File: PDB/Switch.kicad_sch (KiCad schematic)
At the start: 27 parts, among them U1 BTH50030-1LUA, U10 BTH50030-1LUA, U11 74LVC1G175, U12 74LVC1G175, U13 TLV809EA29DBZR, U14 LM4040CELT-3.0, U15 LM4040CELT-3.0

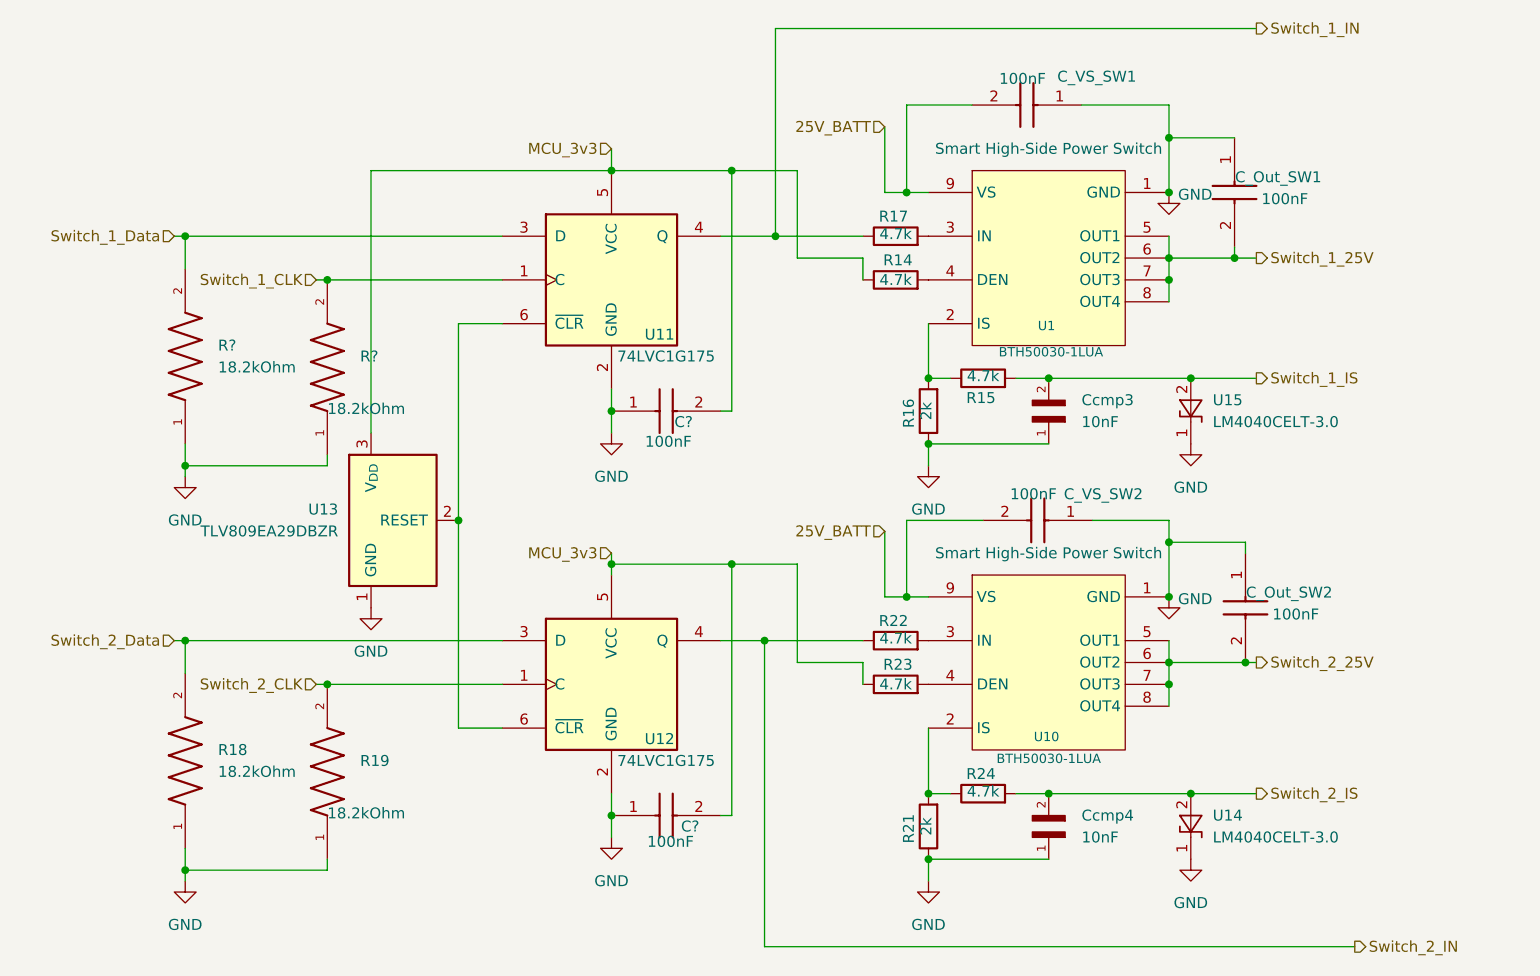
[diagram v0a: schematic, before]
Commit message: sry forgot to push, waiting on PCB shipping atm. Notes: split power distribution into two boards, one for the main 25V distribution, and another for 12V stuff. Also updated CAN transciever. the previous one was a 5V logic one (same logic as its power), and would have fried our ESPs data pins
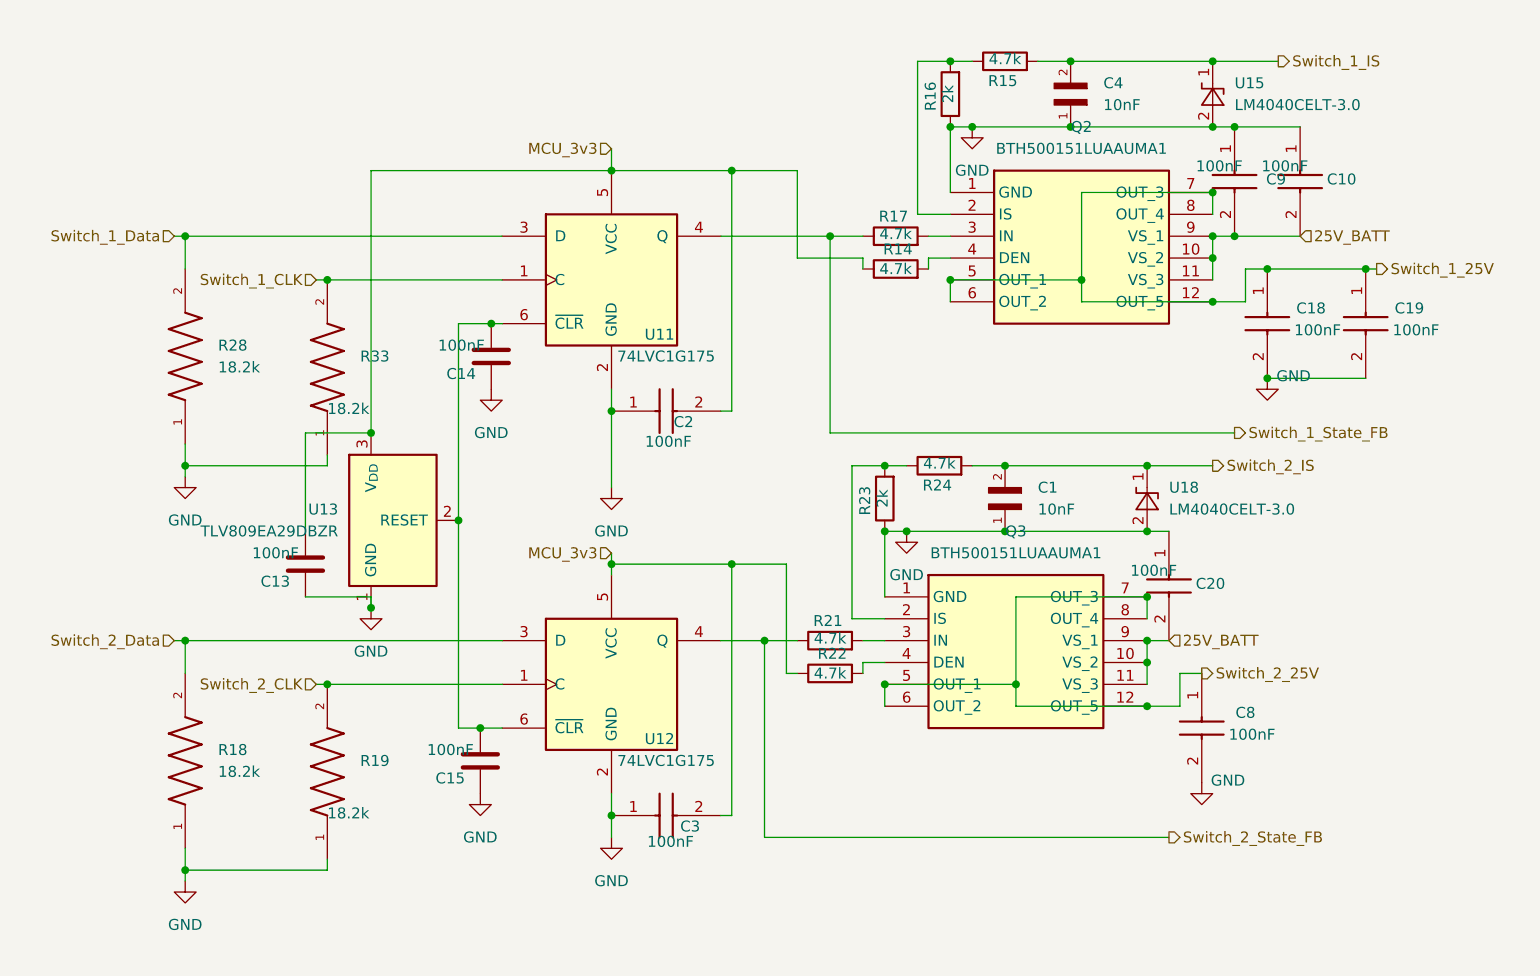
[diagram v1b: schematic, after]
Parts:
- removed C_Out_SW2, C_VS_SW2: 100nF, Capacitor_SMD:C_1206_3216Metric_Pad1.33x1.80mm_HandSolder, symbol 08053C104KAT2A:08053C104KAT2A
- removed Ccmp4: 10nF, Capacitor_SMD:C_1206_3216Metric_Pad1.33x1.80mm_HandSolder, symbol C0805C122J5GACTU:C0805C122J5GACTU
- removed U1, U10: BTH50030-1LUA, BTH500301LUAAUMA1:IFX-PG-HSOF-8-6-V, symbol BTH50030-1LUA:BTH50030-1LUA
- removed U14: LM4040CELT-3.0, Package_TO_SOT_SMD:SOT-23, symbol Reference_Voltage:LM4040DBZ-3
- added C1: 10nF, Capacitor_SMD:C_0805_2012Metric_Pad1.18x1.45mm_HandSolder, symbol C0805C122J5GACTU:C0805C122J5GACTU
- added C10, C19, C20, C8: 100nF, Capacitor_SMD:C_0805_2012Metric_Pad1.18x1.45mm_HandSolder, symbol 08053C104KAT2A:08053C104KAT2A
- added C13, C14, C15: 100nF, Capacitor_SMD:C_0805_2012Metric_Pad1.18x1.45mm_HandSolder, symbol PROVE:1206B104K500CT
- added Q2, Q3: BTH500151LUAAUMA1, PROVE-footprints:BTS500101LUA, symbol PROVE_Symbols:BTH500301LUAAUMA1
- added U18: LM4040CELT-3.0, Package_TO_SOT_SMD:SOT-23, symbol Reference_Voltage:LM4040DBZ-3
- C18: renamed from C_Out_SW1; footprint Capacitor_SMD:C_1206_3216Metric_Pad1.33x1.80mm_HandSolder -> Capacitor_SMD:C_0805_2012Metric_Pad1.18x1.45mm_HandSolder; Purchase Link https://www.mouser.com/en/ProductDetail/KEMET/C1206X104K5RA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 -> https://www.mouser.com/en/ProductDetail/KEMET/C0805X104K1RA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; Specs Cap: 100 nF. VDC: 50. Tolerance 10.0% V -> 100 nF, 100 V, X7R, ±10%
- C2, C3: renamed from C?; footprint Capacitor_SMD:C_1206_3216Metric_Pad1.33x1.80mm_HandSolder -> Capacitor_SMD:C_0805_2012Metric_Pad1.18x1.45mm_HandSolder; Purchase Link https://www.mouser.com/en/ProductDetail/KEMET/C1206X104K5RA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 -> https://www.mouser.com/en/ProductDetail/KEMET/C0805X104K1RA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; Specs Cap: 100 nF. VDC: 50. Tolerance 10.0% V -> 100 nF, 100 V, X7R, ±10%
- C4: renamed from Ccmp3; footprint Capacitor_SMD:C_1206_3216Metric_Pad1.33x1.80mm_HandSolder -> Capacitor_SMD:C_0805_2012Metric_Pad1.18x1.45mm_HandSolder; Purchase Link (none) -> https://www.mouser.com/en/ProductDetail/KEMET/C0805C103J5GA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; Specs Cap: 10 nF (replacing 12nF). VDC: 500V Tolerance 5.0% -> 10 nF, 50 V, C0G/NP0, ±5%
- C9: renamed from C_VS_SW1; footprint Capacitor_SMD:C_1206_3216Metric_Pad1.33x1.80mm_HandSolder -> Capacitor_SMD:C_0805_2012Metric_Pad1.18x1.45mm_HandSolder; Purchase Link https://www.mouser.com/en/ProductDetail/KEMET/C1206X104K5RA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 -> https://www.mouser.com/en/ProductDetail/KEMET/C0805X104K1RA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; Specs Cap: 100 nF. VDC: 50. Tolerance 10.0% V -> 100 nF, 100 V, X7R, ±10%
- R14, R15, R17, R22, R24: footprint Resistor_SMD:R_1206_3216Metric_Pad1.30x1.75mm_HandSolder -> Resistor_SMD:R_0805_2012Metric_Pad1.20x1.40mm_HandSolder; Purchase Link https://www.mouser.com/en/ProductDetail/Vishay/CRCW12064K70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 -> https://www.mouser.com/en/ProductDetail/Vishay/CRCW08054K70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; Specs (none) -> 4.7 kΩ, ±1%, AEC-Q200
- R16: footprint Resistor_SMD:R_1206_3216Metric_Pad1.30x1.75mm_HandSolder -> Resistor_SMD:R_0805_2012Metric_Pad1.20x1.40mm_HandSolder; Purchase Link https://www.mouser.com/en/ProductDetail/Vishay/CRCW12062K00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 -> https://www.mouser.com/en/ProductDetail/Vishay/CRCW08052K00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; Specs (none) -> 2.00 kΩ, ±1%, AEC-Q200
- R18, R19: value 18.2kOhm -> 18.2k; footprint Resistor_SMD:R_1206_3216Metric_Pad1.30x1.75mm_HandSolder -> Resistor_SMD:R_0805_2012Metric_Pad1.20x1.40mm_HandSolder; Purchase Link https://www.mouser.com/en/ProductDetail/Vishay/CRCW120618K2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 -> https://www.mouser.com/en/ProductDetail/Vishay/CRCW080518K2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; Specs Resistance: 18.2 kΩ (replacing 15.4k) Tolerance: 1.0% Power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 -> 18.2 kΩ, ±1%
- R21: value 2k -> 4.7k; footprint Resistor_SMD:R_1206_3216Metric_Pad1.30x1.75mm_HandSolder -> Resistor_SMD:R_0805_2012Metric_Pad1.20x1.40mm_HandSolder; Purchase Link https://www.mouser.com/en/ProductDetail/Vishay/CRCW12062K00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 -> https://www.mouser.com/en/ProductDetail/Vishay/CRCW08054K70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; Specs (none) -> 4.7 kΩ, ±1%, AEC-Q200
- R23: value 4.7k -> 2k; footprint Resistor_SMD:R_1206_3216Metric_Pad1.30x1.75mm_HandSolder -> Resistor_SMD:R_0805_2012Metric_Pad1.20x1.40mm_HandSolder; Purchase Link https://www.mouser.com/en/ProductDetail/Vishay/CRCW12064K70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 -> https://www.mouser.com/en/ProductDetail/Vishay/CRCW08052K00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; Specs (none) -> 2.00 kΩ, ±1%, AEC-Q200
- R28, R33: renamed from R?; value 18.2kOhm -> 18.2k; footprint Resistor_SMD:R_1206_3216Metric_Pad1.30x1.75mm_HandSolder -> Resistor_SMD:R_0805_2012Metric_Pad1.20x1.40mm_HandSolder; Purchase Link https://www.mouser.com/en/ProductDetail/Vishay/CRCW120618K2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 -> https://www.mouser.com/en/ProductDetail/Vishay/CRCW080518K2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; Specs Resistance: 18.2 kΩ (replacing 15.4k) Tolerance: 1.0% Power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 -> 18.2 kΩ, ±1%
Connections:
- net 25V_BATT: now also C10.2, C20.2, Q2.10 (VS_2), Q2.11 (VS_3), Q2.9 (VS_1), Q3.10 (VS_2), Q3.11 (VS_3), Q3.9 (VS_1)
- net GND: now also C18.2, R23.1, U15.2 (A), C1.1, C10.1, C13.2, C14.2, C15.2, C19.2, C20.1, C8.2, Q2.1 (GND), Q3.1 (GND), U18.2 (A); no longer C18.1, R21.1, U15.1 (K)
- net MCU_3v3: now also R22.1, C13.1; no longer R23.1
- net Switch_1_25V: now also C18.1, C19.1, Q2.12 (OUT_5), Q2.5 (OUT_1), Q2.6 (OUT_2), Q2.7 (OUT_3), Q2.8 (OUT_4); no longer C18.2
- net Switch_1_IS: now also U15.1 (K); no longer U15.2 (A)
- net Switch_2_25V: now also C8.1, Q3.12 (OUT_5), Q3.5 (OUT_1), Q3.6 (OUT_2), Q3.7 (OUT_3), Q3.8 (OUT_4)
- net Switch_2_IS: now also C1.2, U18.1 (K)
- net at R24.1: now also R23.2, Q3.2 (IS); no longer R21.2
- net at R17.2: now also Q2.3 (IN)
- net at U11.6 (~{CLR}), U12.6 (~{CLR}), U13.2 (RESET): now also C14.1, C15.1
- net at R14.2: now also Q2.4 (DEN)
- net at R22.2: now also Q3.4 (DEN)
- net at R15.1, R16.2: now also Q2.2 (IS)
- net Switch_1_IN renamed Switch_1_State_FB
- net Switch_2_IN renamed Switch_2_State_FB
- net Switch_2_State_FB: now also R21.1; no longer R22.1
- new net: Q3.3 (IN), R21.2
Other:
- moved on the sheet: C18, C4, C9, R14, R15, R16, U15
